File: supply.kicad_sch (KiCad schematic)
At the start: 54 parts, among them J7 BarrelJack_Pin2mm_MJ-179PH, J8 JST_SH_1x4_BM04B-SRSS-TB-LF-SN, Q12 SI7613DN-T1-GE3, Q13 SI7613DN-T1-GE3, Q14 BSS138PW, Q15 BSS138PW, Q16 BSS138PW, Q17 BSS138PW, SW4 SW_CVS-08TB, SW5 SW_KMR211NGLFS_SMD, U17 LTC4412IS6, U18 LTC4412IS6, U21 NCP718BSN330T1G, U22 MAX16150A_SOT, U26 MAX812REUS+T, U29 AT24CS01_SOT23, U31 LM3880

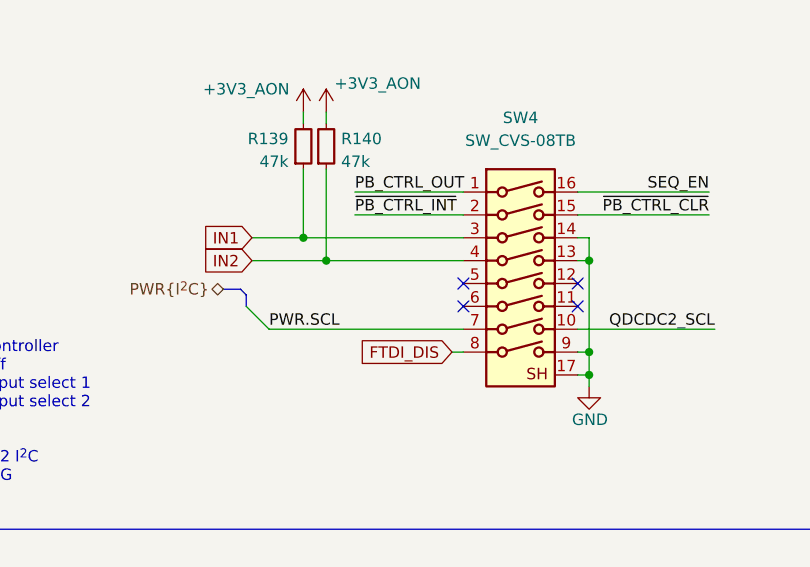
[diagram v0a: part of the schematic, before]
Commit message: [#66727] Minor schematic improvements. Finish routing right side of the board
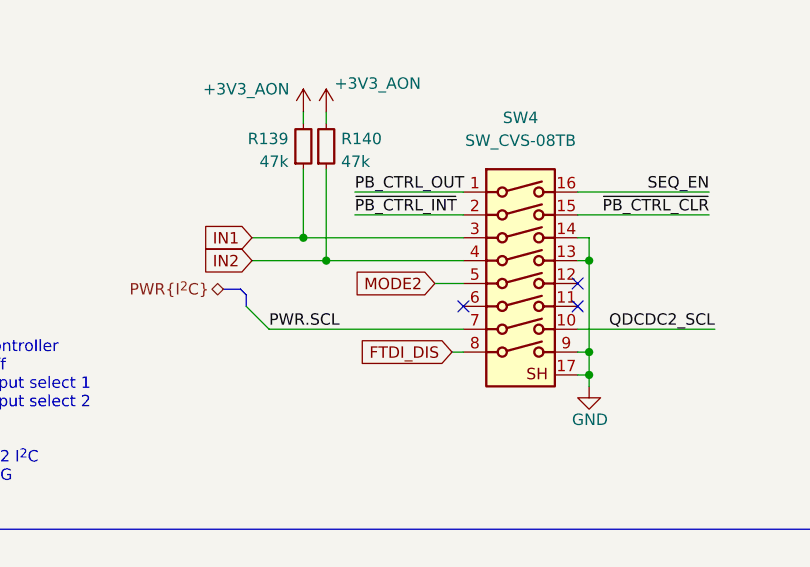
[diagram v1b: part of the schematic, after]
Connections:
- net MODE2: now reaches SW4.5
- no-connect marks 7 -> 6
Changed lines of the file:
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@@
   )
   (no_connect (at 97.155 115.57))
-  (no_connect (at 84.455 115.57))
   (no_connect (at 128.905 264.795))
   (no_connect (at 85.725 70.485))
@@
     (stroke (width 0) (type default))
   )
+  (wire (pts (xy 81.28 115.57) (xy 84.455 115.57))
+    (stroke (width 0) (type default))
+  )
   (wire (pts (xy 95.885 65.405) (xy 95.885 67.945))
     (stroke (width 0) (type default))
@@
     )
   )
+  (global_label "MODE2" (shape input) (at 81.28 115.57 180) (fields_autoplaced)
+    (effects (font (size 1.27 1.27)) (justify right))
+    (property "Intersheetrefs" "${INTERSHEET_REFS}" (at 72.5386 115.57 0)
+      (effects (font (size 1.27 1.27)) (justify right))
+    )
+  )

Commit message: [#67725] Update power supply sheet
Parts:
- removed J7: BarrelJack_Pin2mm_MJ-179PH, antmicro-footprints:BarrelJack_Pin2mm_MJ-179PH, symbol antmicroBarrelPowerConnectors:BarrelJack_Pin2mm_MJ-179PH
- added J7: BarrelJack_Pin1.3mm_694103107102, antmicro-footprints:BarrelJack_Pin1.3mm_694103107102, symbol antmicroBarrelPowerConnectors:BarrelJack_Pin1.3mm_694103107102
- D16: footprint antmicro-footprints:ESDA25P35-1U1M -> antmicro-footprints:QFN-2L_1.6x1x0.55mm
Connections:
- net 12V_aux: now also J7.1
- net 12V_aux_fused: now also D16.1 (C); no longer D16.2 (A)
- net GND: now also D16.2 (A), J7.2, J7.3; no longer D16.1 (K)
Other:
- note added: "Power supply"
- moved on the sheet: C169, C170, C175, C176, C179, C180, C181, C194, C195, C198, C203, C207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

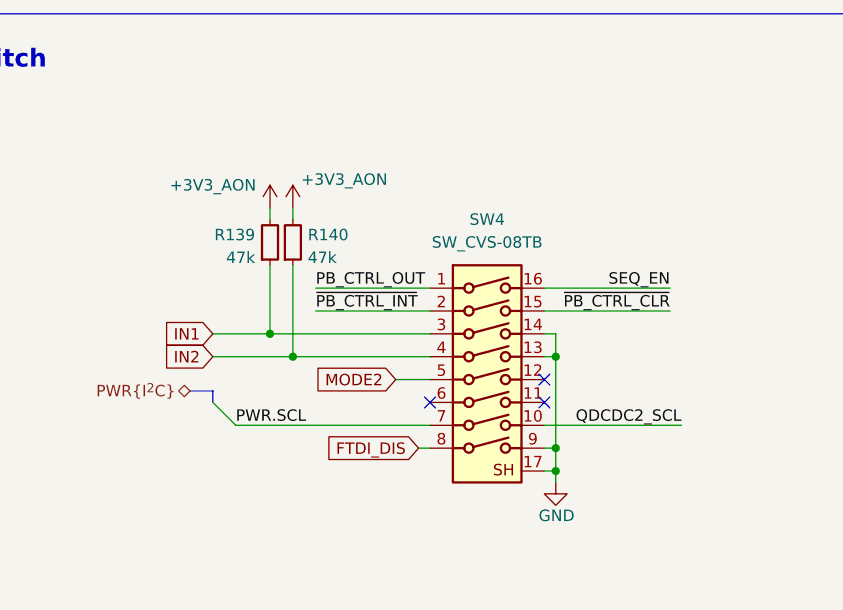
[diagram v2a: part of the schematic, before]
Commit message: [#67725] Clean-up fpga-config sheet
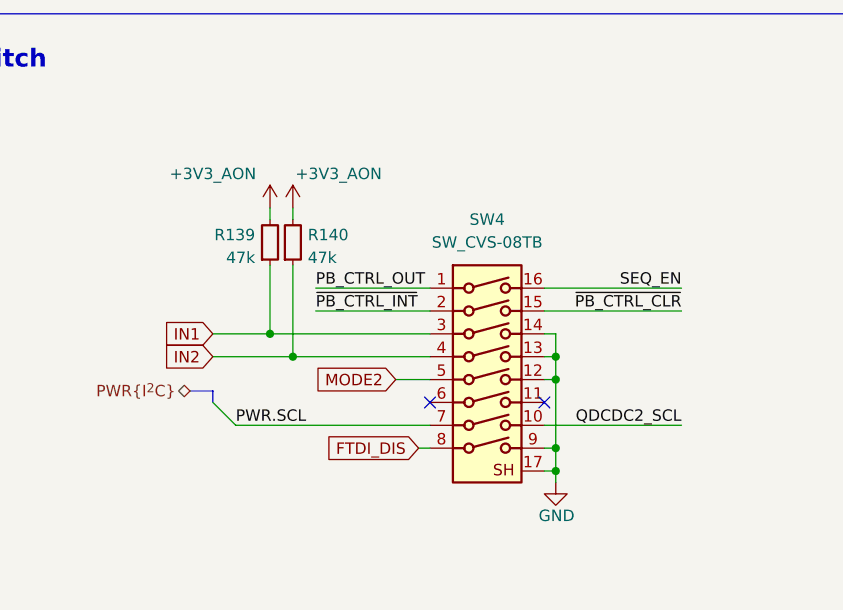
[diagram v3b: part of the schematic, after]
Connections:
- net GND: now also SW4.12
- no-connect marks 6 -> 5
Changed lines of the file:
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@@
   (junction (at 290.83 182.88) (diameter 0) (color 0 0 0 0)
   )
+  (junction (at 92.71 233.68) (diameter 0) (color 0 0 0 0)
+  )
   (junction (at 204.47 64.77) (diameter 0) (color 0 0 0 0)
   )
@@
   (junction (at 130.81 87.63) (diameter 0) (color 0 0 0 0)
   )
-  (no_connect (at 91.44 233.68))
   (no_connect (at 358.14 64.77))
   (no_connect (at 105.41 92.71))
@@
     (stroke (width 0) (type default))
   )
-  (wire (pts (xy 92.71 241.3) (xy 92.71 231.14))
+  (wire (pts (xy 92.71 241.3) (xy 92.71 233.68))
     (stroke (width 0) (type default))
   )
@@
     (stroke (width 0) (type default))
   )
-  (wire (pts (xy 105.41 223.52) (xy 91.44 223.52))
+  (wire (pts (xy 91.44 223.52) (xy 106.68 223.52))
     (stroke (width 0) (type default))
   )
@@
     (stroke (width 0) (type default))
   )
-  (wire (pts (xy 105.41 226.06) (xy 91.44 226.06))
+  (wire (pts (xy 91.44 226.06) (xy 106.68 226.06))
     (stroke (width 0) (type default))
   )
@@
     (stroke (width 0) (type default))
   )
+  (wire (pts (xy 92.71 233.68) (xy 92.71 231.14))
+    (stroke (width 0) (type default))
+  )
   (wire (pts (xy 262.89 167.64) (xy 278.13 167.64))
     (stroke (width 0) (type default))
@@
     (stroke (width 0) (type default))
   )
+  (wire (pts (xy 91.44 233.68) (xy 92.71 233.68))
+    (stroke (width 0) (type default))
+  )
   (wire (pts (xy 229.87 176.53) (xy 229.87 180.34))
     (stroke (width 0) (type default))
@@
     (effects (font (size 1.27 1.27)) (justify left bottom))
   )
-  (label "~{PB_CTRL_CLR}" (at 105.41 226.06 180) (fields_autoplaced)
+  (label "~{PB_CTRL_CLR}" (at 106.68 226.06 180) (fields_autoplaced)
     (effects (font (size 1.27 1.27)) (justify right bottom))
   )
@@
     (effects (font (size 1.27 1.27)) (justify left bottom))
   )
-  (label "SEQ_EN" (at 105.41 223.52 180) (fields_autoplaced)
+  (label "SEQ_EN" (at 106.68 223.52 180) (fields_autoplaced)
     (effects (font (size 1.27 1.27)) (justify right bottom))
   )
@@
       (effects (font (size 1.27 1.27)) hide)
     )
-    (property "Value" "+3V3_AON" (at 69.215 211.455 0)
+    (property "Value" "+3V3_AON" (at 68.58 210.82 0)
       (effects (font (size 1.27 1.27)))
     )
@@
       (effects (font (size 1.27 1.27)) hide)
     )
-    (property "Value" "+3V3_AON" (at 54.61 212.09 0)
+    (property "Value" "+3V3_AON" (at 54.61 210.82 0)
       (effects (font (size 1.27 1.27)))
     )

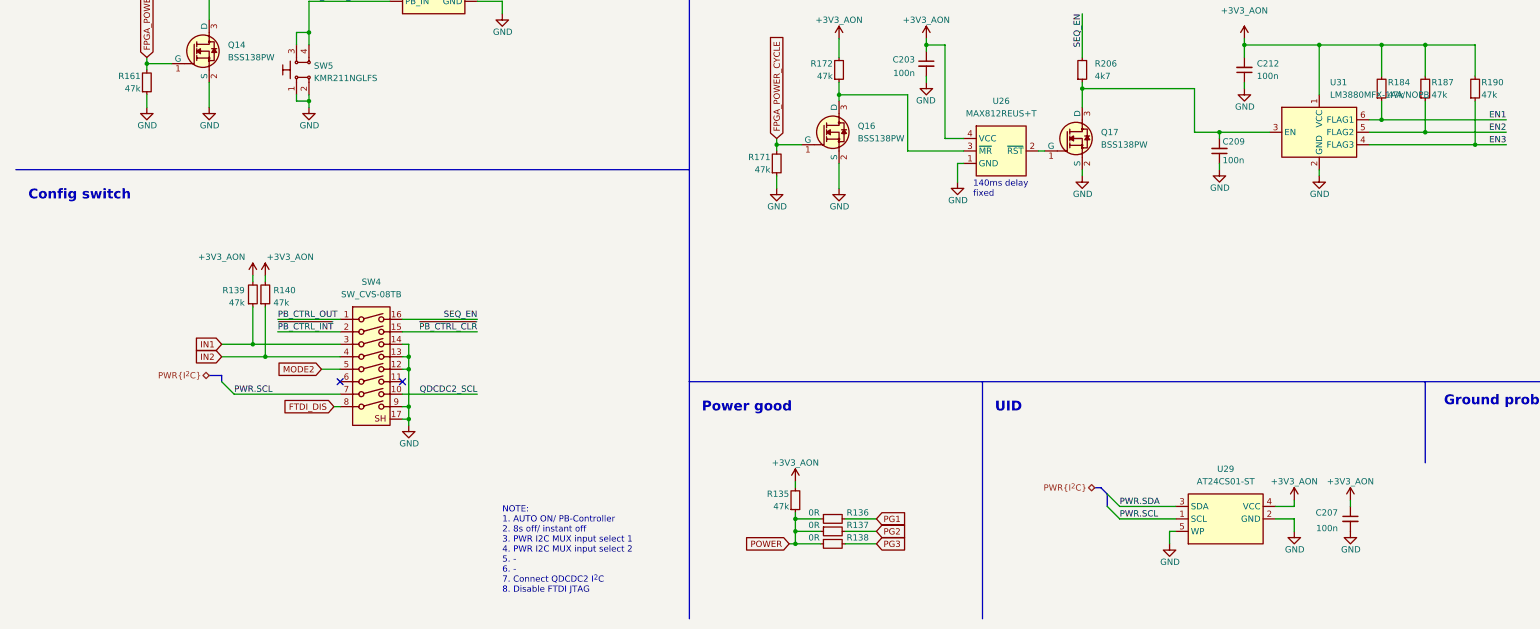
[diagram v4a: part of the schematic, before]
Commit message: [#68016] Improve bus entry marking
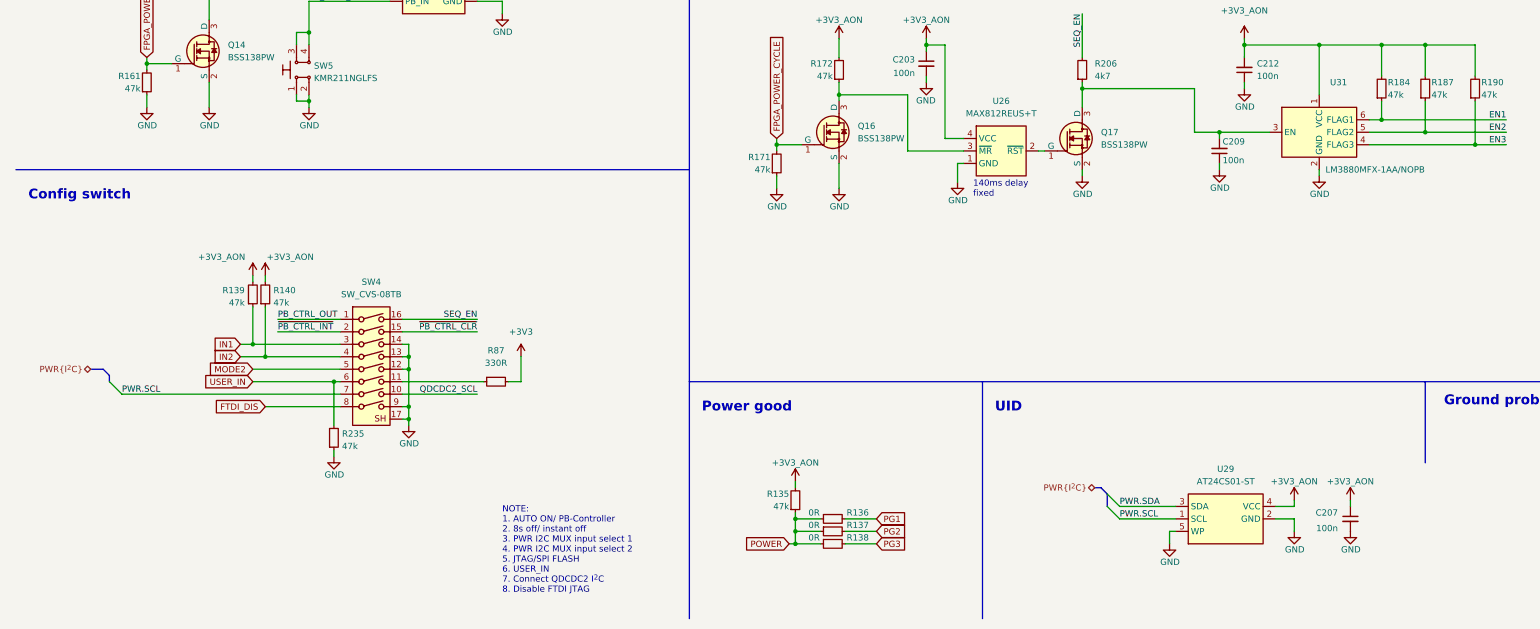
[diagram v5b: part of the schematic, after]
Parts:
- added R235: R_47k_0402, antmicro-footprints:R_0402_1005Metric, symbol antmicroResistors0402:R_47k_0402
- added R87: R_330R_0402, antmicro-footprints:R_0402_1005Metric, symbol antmicroResistors0402:R_330R_0402
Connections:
- net GND: now also R235.1
- net at SW4.11: now also R87.1
- net USER_IN: now reaches SW4.6
- net USER_IN: now also R235.2
- new net +3V3: R87.2
- no-connect marks 5 -> 3
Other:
- note added: "NOTE: 1. AUTO ON/ PB-Controller 2. 8s off/ instant off 3. PWR I2C MUX input select 1 4. PWR I2C MUX input select 2 5. JTAG/SPI FLASH 6. USER_IN 7. Connect QDCDC2 I^{2}C 8. Disable FTDI JTAG"
- note removed: "NOTE: 1. AUTO ON/ PB-Controller 2. 8s off/ instant off 3. PWR I2C MUX input select 1 4. PWR I2C MUX input select 2 5. - 6. - 7. Connect QDCDC2 I^{2}C 8. Disable FTDI JTAG"

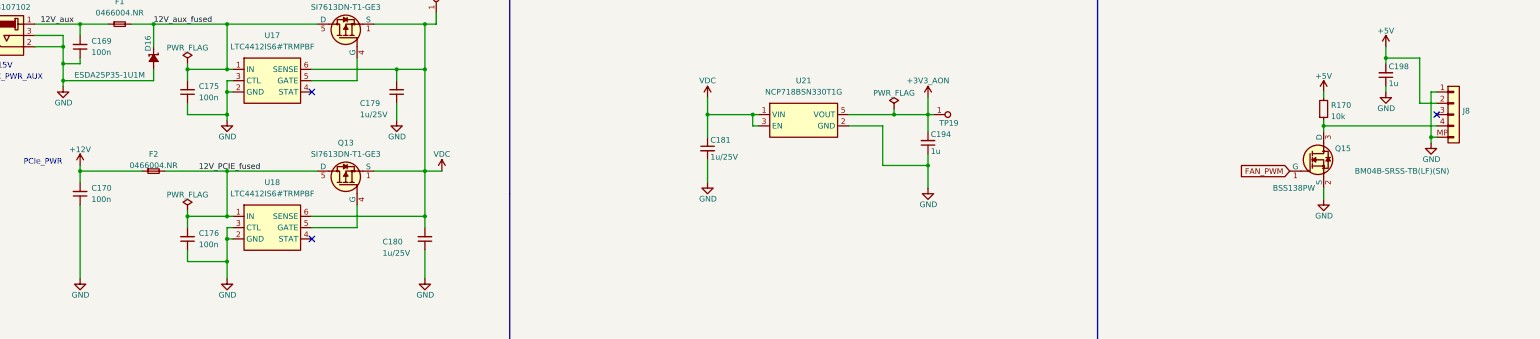
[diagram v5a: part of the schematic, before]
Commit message: [#68016] Solve ERC warrings and errors
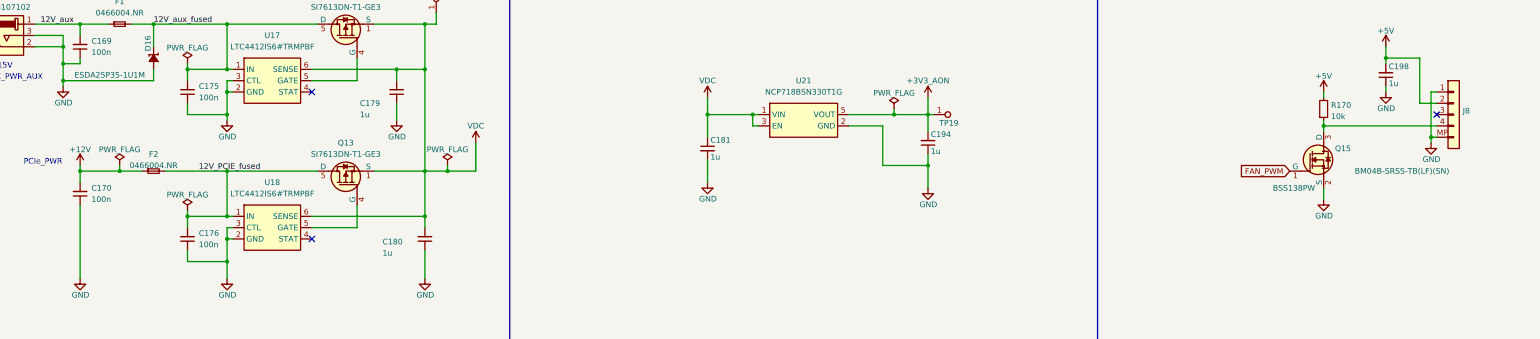
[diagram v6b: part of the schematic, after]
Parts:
- C179, C180, C181: Val 1u/25V -> 1u; Voltage (none) -> 25V
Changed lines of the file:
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@@
   (junction (at 86.36 54.61) (diameter 0) (color 0 0 0 0)
   )
+  (junction (at 135.89 77.47) (diameter 0) (color 0 0 0 0)
+  )
   (junction (at 354.33 157.48) (diameter 0) (color 0 0 0 0)
   )
@@
   (junction (at 39.37 171.45) (diameter 0) (color 0 0 0 0)
   )
+  (junction (at 62.23 77.47) (diameter 0) (color 0 0 0 0)
+  )
   (junction (at 130.81 44.45) (diameter 0) (color 0 0 0 0)
   )
@@
     (stroke (width 0) (type default))
   )
+  (wire (pts (xy 135.89 76.2) (xy 135.89 77.47))
+    (stroke (width 0) (type default))
+  )
   (wire (pts (xy 262.89 175.26) (xy 262.89 176.53))
     (stroke (width 0) (type default))
@@
     (stroke (width 0) (type default))
   )
+  (wire (pts (xy 135.89 77.47) (xy 142.24 77.47))
+    (stroke (width 0) (type default))
+  )
   (wire (pts (xy 167.64 187.96) (xy 167.64 189.23))
     (stroke (width 0) (type default))
@@
     (stroke (width 0) (type default))
   )
-  (wire (pts (xy 53.34 77.47) (xy 67.31 77.47))
+  (wire (pts (xy 53.34 77.47) (xy 62.23 77.47))
     (stroke (width 0) (type default))
   )
@@
     (stroke (width 0) (type default))
   )
+  (wire (pts (xy 62.23 76.2) (xy 62.23 77.47))
+    (stroke (width 0) (type default))
+  )
   (wire (pts (xy 201.93 186.69) (xy 205.74 186.69))
     (stroke (width 0) (type default))
@@
     (stroke (width 0) (type default))
   )
+  (wire (pts (xy 62.23 77.47) (xy 67.31 77.47))
+    (stroke (width 0) (type default))
+  )
   (wire (pts (xy 358.14 59.69) (xy 356.87 59.69))
     (stroke (width 0) (type default))
@@
     (stroke (width 0) (type default))
   )
-  (wire (pts (xy 130.81 77.47) (xy 134.62 77.47))
+  (wire (pts (xy 130.81 77.47) (xy 135.89 77.47))
     (stroke (width 0) (type default))
   )
@@
     (stroke (width 0) (type default))
   )
+  (wire (pts (xy 142.24 71.12) (xy 142.24 77.47))
+    (stroke (width 0) (type default))
+  )
   (wire (pts (xy 77.47 236.22) (xy 78.74 236.22))
     (stroke (width 0) (type default))
@@
     )
   )
-  (symbol (lib_id "antmicropower:VDC") (at 134.62 77.47 0) (unit 1)
+  (symbol (lib_id "antmicropower:VDC") (at 142.24 71.12 0) (unit 1)
     (in_bom yes) (on_board yes) (dnp no)
-    (property "Reference" "#PWR0300" (at 134.62 80.01 0)
+    (property "Reference" "#PWR0300" (at 142.24 73.66 0)
       (effects (font (size 1.27 1.27)) hide)
     )
-    (property "Value" "VDC" (at 134.62 73.66 0)
+    (property "Value" "VDC" (at 142.24 67.31 0)
       (effects (font (size 1.27 1.27)))
     )
-    (property "Footprint" "" (at 134.62 77.47 0)
+    (property "Footprint" "" (at 142.24 71.12 0)
       (effects (font (size 1.27 1.27)) hide)
     )
-    (property "Datasheet" "" (at 134.62 77.47 0)
+    (property "Datasheet" "" (at 142.24 71.12 0)
       (effects (font (size 1.27 1.27)) hide)
     )
@@
     )
   )
+  (symbol (lib_id "antmicropower:PWR_FLAG") (at 62.23 76.2 0) (unit 1)
+    (in_bom yes) (on_board yes) (dnp no) (fields_autoplaced)
+    (property "Reference" "#FLG020" (at 62.23 74.295 0)
+      (effects (font (size 1.27 1.27)) hide)
+    )
+    (property "Value" "PWR_FLAG" (at 62.23 72.6242 0)
+      (effects (font (size 1.27 1.27)))
+    )
+    (property "Footprint" "" (at 62.23 76.2 0)
+      (effects (font (size 1.27 1.27)) hide)
+    )
+    (property "Datasheet" "" (at 62.23 76.2 0)
+      (effects (font (size 1.27 1.27)) hide)
+    )
+    (pin "1")
+    (instances
+      (project "data-center-rdimm-ddr5-tester"
+        (path "/1faa6543-e26a-4449-8bac-ee14b9f19e5f/00000000-0000-0000-0000-000060225b0c"
+          (reference "#FLG020") (unit 1)
+        )
+      )
+    )
+  )
   (symbol (lib_id "antmicroFuses:F_4A_1206") (at 67.31 77.47 0) (unit 1)
     (in_bom yes) (on_board yes) (dnp no) (fields_autoplaced)
@@
     )
   )
+  (symbol (lib_id "antmicropower:PWR_FLAG") (at 135.89 76.2 0) (unit 1)
+    (in_bom yes) (on_board yes) (dnp no) (fields_autoplaced)
+    (property "Reference" "#FLG05" (at 135.89 74.295 0)
+      (effects (font (size 1.27 1.27)) hide)
+    )
+    (property "Value" "PWR_FLAG" (at 135.89 72.6242 0)
+      (effects (font (size 1.27 1.27)))
+    )
+    (property "Footprint" "" (at 135.89 76.2 0)
+      (effects (font (size 1.27 1.27)) hide)
+    )
+    (property "Datasheet" "" (at 135.89 76.2 0)
+      (effects (font (size 1.27 1.27)) hide)
+    )
+    (pin "1")
+    (instances
+      (project "data-center-rdimm-ddr5-tester"
+        (path "/1faa6543-e26a-4449-8bac-ee14b9f19e5f/00000000-0000-0000-0000-000060225b0c"
+          (reference "#FLG05") (unit 1)
+        )
+      )
+    )
+  )
   (symbol (lib_id "antmicropower:PWR_FLAG") (at 77.47 53.34 0) (unit 1)
     (in_bom yes) (on_board yes) (dnp no)
@@
       (effects (font (size 1.27 1.27) (thickness 0.15)) (justify left bottom) hide)
     )
-    (property "Val" "1u/25V" (at 116.205 64.77 90)
+    (property "Val" "1u" (at 116.205 64.77 90)
       (effects (font (size 1.27 1.27) (thickness 0.15)) (justify right))
     )
@@
       (effects (font (size 1.27 1.27) (thickness 0.15)) (justify left bottom) hide)
     )
-    (property "Voltage" "" (at 152.4 41.91 0)
+    (property "Voltage" "25V" (at 152.4 41.91 0)
       (effects (font (size 1.27 1.27)) (justify left bottom) hide)
     )
@@
       (effects (font (size 1.27 1.27) (thickness 0.15)) (justify left bottom) hide)
     )
-    (property "Val" "1u/25V" (at 194.945 74.295 90)
+    (property "Val" "1u" (at 194.945 74.295 90)
       (effects (font (size 1.27 1.27) (thickness 0.15)) (justify right))
     )
@@
       (effects (font (size 1.27 1.27) (thickness 0.15)) (justify left bottom) hide)
     )
-    (property "Voltage" "" (at 222.25 90.17 0)
+    (property "Voltage" "25V" (at 222.25 90.17 0)
       (effects (font (size 1.27 1.27)) (justify left bottom) hide)
     )
@@
       (effects (font (size 1.27 1.27) (thickness 0.15)) (justify left bottom) hide)
     )
-    (property "Val" "1u/25V" (at 121.285 95.885 90)
+    (property "Val" "1u" (at 121.285 95.885 90)
       (effects (font (size 1.27 1.27) (thickness 0.15)) (justify right))
     )
@@
       (effects (font (size 1.27 1.27) (thickness 0.15)) (justify left bottom) hide)
     )
-    (property "Voltage" "" (at 158.75 74.93 0)
+    (property "Voltage" "25V" (at 158.75 74.93 0)
       (effects (font (size 1.27 1.27)) (justify left bottom) hide)
     )
